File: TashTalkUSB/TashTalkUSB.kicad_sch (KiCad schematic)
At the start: 32 parts, among them J1 TC2030, J3 USB_C_Receptacle_USB2.0_14P, U1 CP2102N-Axx-xQFN20, U2 PIC12F1840-xSN, U3 SN65HVD1473DGSR

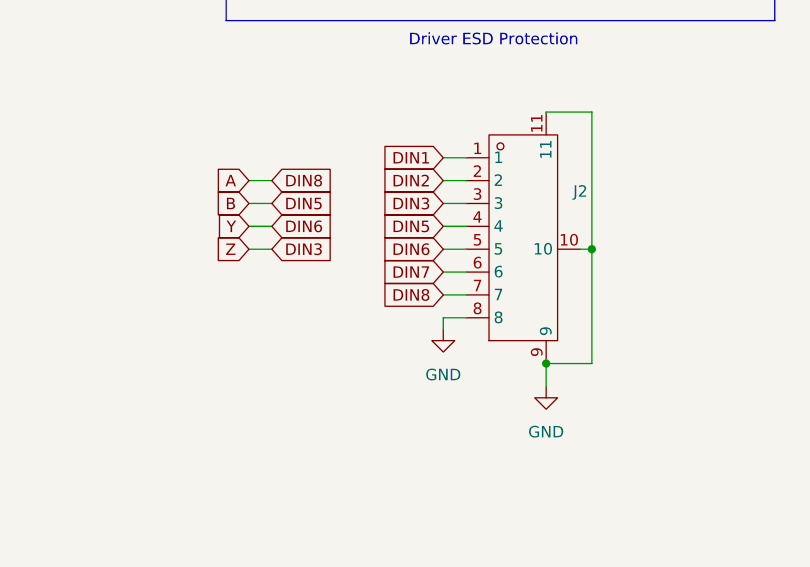
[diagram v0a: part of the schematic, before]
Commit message: Fix InkTalk and TashTalk USB flipped DIN pins
I accidentally transposed DIN7 and DIN8 when wiring up the connector
in KiCAD (yay weird pin choices on connectors). This explains the rather
odd and unexplainable cases of TashTalk USB not liking resistor pins
on PhoneNET connectors and long cables. It additionally caused InkTalk
to not work at all with the Colour StyleWriter 2200.

Easy fix thankfullly - commit contains just that flip around and some
minor board clean up for the first production-ish run of InkTalk.
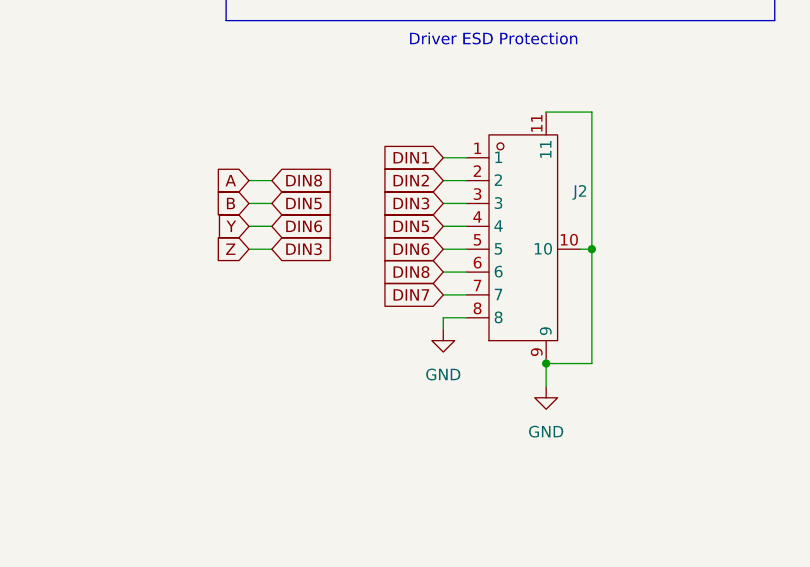
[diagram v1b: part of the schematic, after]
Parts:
- J2: value ~ -> (none)
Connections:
- net A: now also J2.6; no longer J2.7
- net DIN7: now also J2.7; no longer J2.6
